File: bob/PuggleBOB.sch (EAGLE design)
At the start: 9 parts

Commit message: Fixed the ribbon cable mapping to take into account reflective symmetry.
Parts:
- A_I/O: value PINHD-2X5/90 -> PINHD-2X5; device adafruit:PINHD-2X5/90 -> adafruit:PINHD-2X5
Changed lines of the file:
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@@
 </classes>
 <parts>
-<part name="A_I/O" library="adafruit" deviceset="PINHD-2X5" device="/90"/>
+<part name="A_I/O" library="adafruit" deviceset="PINHD-2X5" device="" value="PINHD-2X5"/>
 <part name="AI_0" library="con-coax" deviceset="BN35N61" device="" value="5-1634503-1"/>
 <part name="AI_1" library="con-coax" deviceset="BN35N61" device="" value="5-1634503-1"/>

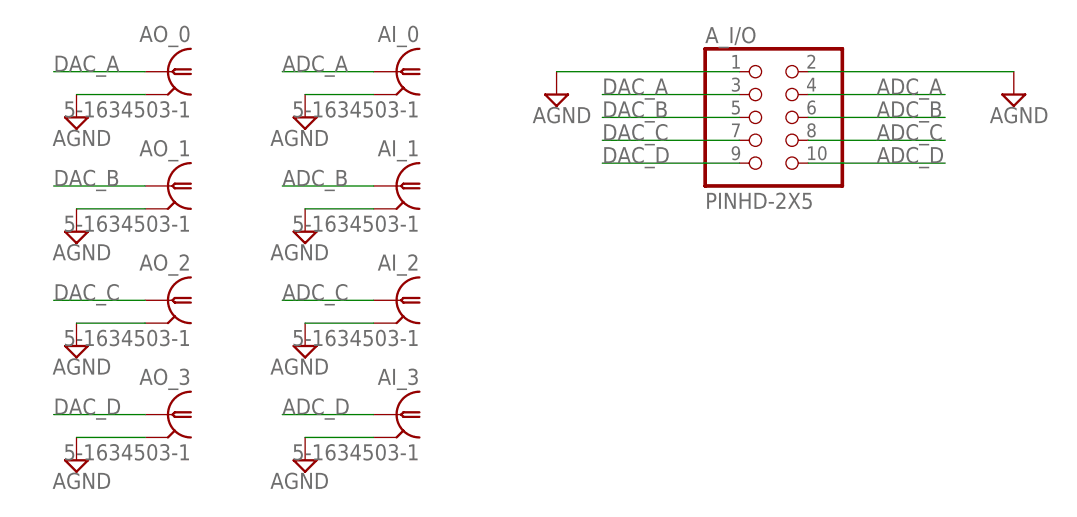
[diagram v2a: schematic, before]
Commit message: Silkscreen changes.
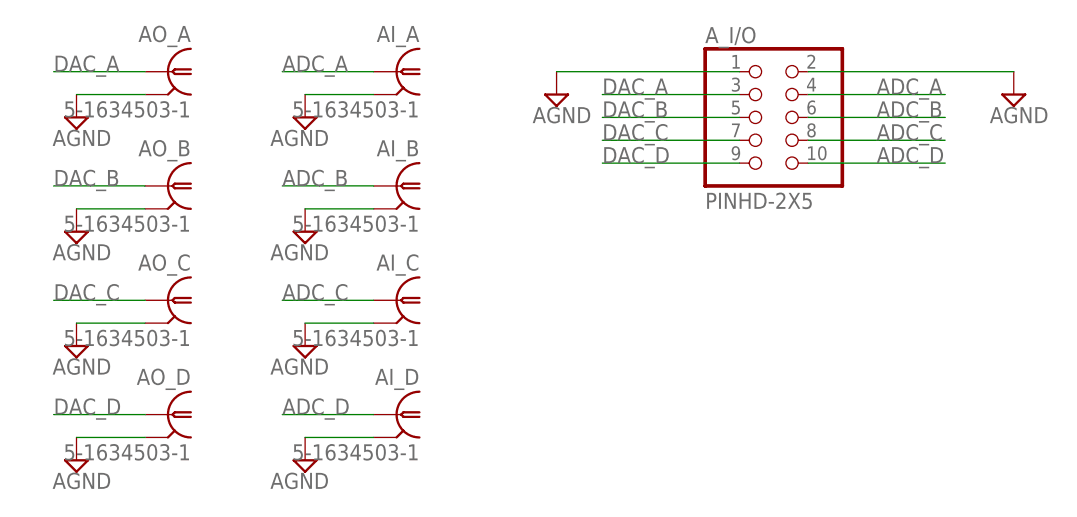
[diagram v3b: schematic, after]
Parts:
- renumbered AI_0 to AI_A, AI_1 to AI_B, AI_2 to AI_C, AI_3 to AI_D, AO_0 to AO_A, AO_1 to AO_B, AO_2 to AO_C, AO_3 to AO_D
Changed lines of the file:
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@@
 <parts>
 <part name="A_I/O" library="adafruit" deviceset="PINHD-2X5" device="" value="PINHD-2X5"/>
-<part name="AI_0" library="con-coax" deviceset="BN35N61" device="" value="5-1634503-1"/>
-<part name="AI_1" library="con-coax" deviceset="BN35N61" device="" value="5-1634503-1"/>
-<part name="AI_2" library="con-coax" deviceset="BN35N61" device="" value="5-1634503-1"/>
-<part name="AI_3" library="con-coax" deviceset="BN35N61" device="" value="5-1634503-1"/>
-<part name="AO_0" library="con-coax" deviceset="BN35N61" device="" value="5-1634503-1"/>
-<part name="AO_1" library="con-coax" deviceset="BN35N61" device="" value="5-1634503-1"/>
-<part name="AO_2" library="con-coax" deviceset="BN35N61" device="" value="5-1634503-1"/>
-<part name="AO_3" library="con-coax" deviceset="BN35N61" device="" value="5-1634503-1"/>
+<part name="AI_A" library="con-coax" deviceset="BN35N61" device="" value="5-1634503-1"/>
+<part name="AI_B" library="con-coax" deviceset="BN35N61" device="" value="5-1634503-1"/>
+<part name="AI_C" library="con-coax" deviceset="BN35N61" device="" value="5-1634503-1"/>
+<part name="AI_D" library="con-coax" deviceset="BN35N61" device="" value="5-1634503-1"/>
+<part name="AO_A" library="con-coax" deviceset="BN35N61" device="" value="5-1634503-1"/>
+<part name="AO_B" library="con-coax" deviceset="BN35N61" device="" value="5-1634503-1"/>
+<part name="AO_C" library="con-coax" deviceset="BN35N61" device="" value="5-1634503-1"/>
+<part name="AO_D" library="con-coax" deviceset="BN35N61" device="" value="5-1634503-1"/>
 <part name="SUPPLY1" library="supply2" deviceset="AGND" device=""/>
 <part name="SUPPLY2" library="supply2" deviceset="AGND" device=""/>
@@
 <instances>
 <instance part="A_I/O" gate="G$1" x="68.58" y="48.26"/>
-<instance part="AI_0" gate="G$1" x="27.94" y="50.8" rot="MR0"/>
-<instance part="AI_1" gate="G$1" x="27.94" y="38.1" rot="MR0"/>
-<instance part="AI_2" gate="G$1" x="27.94" y="25.4" rot="MR0"/>
-<instance part="AI_3" gate="G$1" x="27.94" y="12.7" rot="MR0"/>
-<instance part="AO_0" gate="G$1" x="2.54" y="50.8" rot="MR0"/>
-<instance part="AO_1" gate="G$1" x="2.54" y="38.1" rot="MR0"/>
-<instance part="AO_2" gate="G$1" x="2.54" y="25.4" rot="MR0"/>
-<instance part="AO_3" gate="G$1" x="2.54" y="12.7" rot="MR0"/>
+<instance part="AI_A" gate="G$1" x="27.94" y="50.8" rot="MR0"/>
+<instance part="AI_B" gate="G$1" x="27.94" y="38.1" rot="MR0"/>
+<instance part="AI_C" gate="G$1" x="27.94" y="25.4" rot="MR0"/>
+<instance part="AI_D" gate="G$1" x="27.94" y="12.7" rot="MR0"/>
+<instance part="AO_A" gate="G$1" x="2.54" y="50.8" rot="MR0"/>
+<instance part="AO_B" gate="G$1" x="2.54" y="38.1" rot="MR0"/>
+<instance part="AO_C" gate="G$1" x="2.54" y="25.4" rot="MR0"/>
+<instance part="AO_D" gate="G$1" x="2.54" y="12.7" rot="MR0"/>
 <instance part="SUPPLY1" gate="G$1" x="17.78" y="7.62" rot="MR0"/>
 <instance part="SUPPLY2" gate="G$1" x="17.78" y="20.32" rot="MR0"/>
@@
 <net name="AGND" class="0">
 <segment>
-<pinref part="AI_3" gate="G$1" pin="2"/>
+<pinref part="AI_D" gate="G$1" pin="2"/>
 <pinref part="SUPPLY1" gate="G$1" pin="AGND"/>
 <wire x1="25.4" y1="10.16" x2="17.78" y2="10.16" width="0.1524" layer="91"/>
 </segment>
 <segment>
-<pinref part="AI_2" gate="G$1" pin="2"/>
+<pinref part="AI_C" gate="G$1" pin="2"/>
 <pinref part="SUPPLY2" gate="G$1" pin="AGND"/>
 <wire x1="25.4" y1="22.86" x2="17.78" y2="22.86" width="0.1524" layer="91"/>
 </segment>
 <segment>
-<pinref part="AI_1" gate="G$1" pin="2"/>
+<pinref part="AI_B" gate="G$1" pin="2"/>
 <pinref part="SUPPLY3" gate="G$1" pin="AGND"/>
 <wire x1="25.4" y1="35.56" x2="17.78" y2="35.56" width="0.1524" layer="91"/>
 </segment>
 <segment>
-<pinref part="AI_0" gate="G$1" pin="2"/>
+<pinref part="AI_A" gate="G$1" pin="2"/>
 <wire x1="25.4" y1="48.26" x2="17.78" y2="48.26" width="0.1524" layer="91"/>
 <pinref part="SUPPLY4" gate="G$1" pin="AGND"/>
@@
 <segment>
 <pinref part="SUPPLY7" gate="G$1" pin="AGND"/>
-<pinref part="AO_0" gate="G$1" pin="2"/>
+<pinref part="AO_A" gate="G$1" pin="2"/>
 <wire x1="-7.62" y1="48.26" x2="0" y2="48.26" width="0.1524" layer="91"/>
 </segment>
 <segment>
 <pinref part="SUPPLY8" gate="G$1" pin="AGND"/>
-<pinref part="AO_1" gate="G$1" pin="2"/>
+<pinref part="AO_B" gate="G$1" pin="2"/>
 <wire x1="-7.62" y1="35.56" x2="0" y2="35.56" width="0.1524" layer="91"/>
 </segment>
 <segment>
 <pinref part="SUPPLY9" gate="G$1" pin="AGND"/>
-<pinref part="AO_2" gate="G$1" pin="2"/>
+<pinref part="AO_C" gate="G$1" pin="2"/>
 <wire x1="-7.62" y1="22.86" x2="0" y2="22.86" width="0.1524" layer="91"/>
 </segment>
 <segment>
 <pinref part="SUPPLY10" gate="G$1" pin="AGND"/>
-<pinref part="AO_3" gate="G$1" pin="2"/>
+<pinref part="AO_D" gate="G$1" pin="2"/>
 <wire x1="-7.62" y1="10.16" x2="0" y2="10.16" width="0.1524" layer="91"/>
 </segment>
@@
 </segment>
 <segment>
-<pinref part="AO_0" gate="G$1" pin="1"/>
+<pinref part="AO_A" gate="G$1" pin="1"/>
 <wire x1="0" y1="50.8" x2="-10.16" y2="50.8" width="0.1524" layer="91"/>
 <label x="-10.16" y="50.8" size="1.778" layer="95"/>
@@
 </segment>
 <segment>
-<pinref part="AO_1" gate="G$1" pin="1"/>
+<pinref part="AO_B" gate="G$1" pin="1"/>
 <wire x1="0" y1="38.1" x2="-10.16" y2="38.1" width="0.1524" layer="91"/>
 <label x="-10.16" y="38.1" size="1.778" layer="95"/>
@@
 </segment>
 <segment>
-<pinref part="AO_2" gate="G$1" pin="1"/>
+<pinref part="AO_C" gate="G$1" pin="1"/>
 <wire x1="0" y1="25.4" x2="-10.16" y2="25.4" width="0.1524" layer="91"/>
 <label x="-10.16" y="25.4" size="1.778" layer="95"/>
@@
 </segment>
 <segment>
-<pinref part="AO_3" gate="G$1" pin="1"/>
+<pinref part="AO_D" gate="G$1" pin="1"/>
 <wire x1="0" y1="12.7" x2="-10.16" y2="12.7" width="0.1524" layer="91"/>
 <label x="-10.16" y="12.7" size="1.778" layer="95"/>
@@
 </segment>
 <segment>
-<pinref part="AI_0" gate="G$1" pin="1"/>
+<pinref part="AI_A" gate="G$1" pin="1"/>
 <wire x1="25.4" y1="50.8" x2="15.24" y2="50.8" width="0.1524" layer="91"/>
 <label x="15.24" y="50.8" size="1.778" layer="95"/>
@@
 </segment>
 <segment>
-<pinref part="AI_1" gate="G$1" pin="1"/>
+<pinref part="AI_B" gate="G$1" pin="1"/>
 <wire x1="25.4" y1="38.1" x2="15.24" y2="38.1" width="0.1524" layer="91"/>
 <label x="15.24" y="38.1" size="1.778" layer="95"/>
@@
 </segment>
 <segment>
-<pinref part="AI_2" gate="G$1" pin="1"/>
+<pinref part="AI_C" gate="G$1" pin="1"/>
 <wire x1="25.4" y1="25.4" x2="15.24" y2="25.4" width="0.1524" layer="91"/>
 <label x="15.24" y="25.4" size="1.778" layer="95"/>
@@
 </segment>
 <segment>
-<pinref part="AI_3" gate="G$1" pin="1"/>
+<pinref part="AI_D" gate="G$1" pin="1"/>
 <wire x1="25.4" y1="12.7" x2="15.24" y2="12.7" width="0.1524" layer="91"/>
 <label x="15.24" y="12.7" size="1.778" layer="95"/>
